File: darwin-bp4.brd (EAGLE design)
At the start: 95 x 128 mm, 25 parts, among them U1 MCP23008, U2 TCA9548A, U3 LP5012

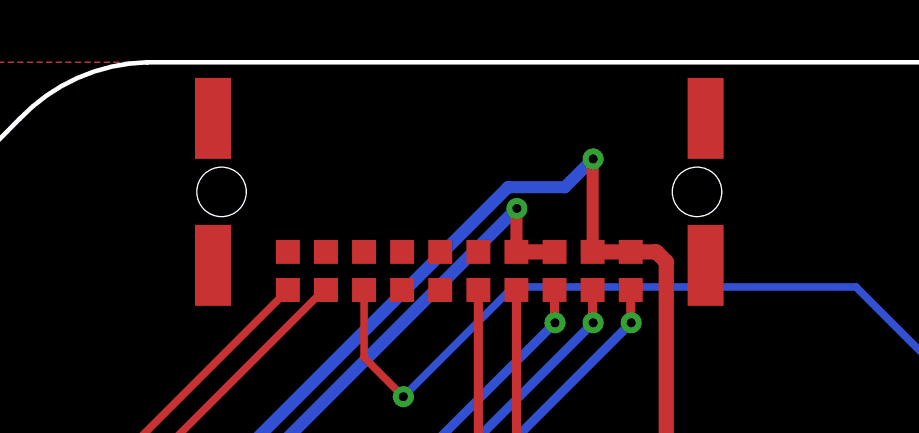
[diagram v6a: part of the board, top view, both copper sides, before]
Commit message: Fixed updated connector footprint.
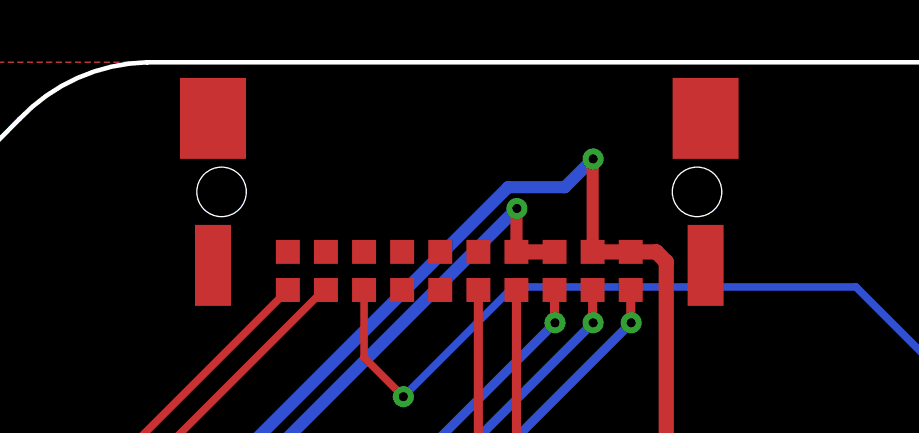
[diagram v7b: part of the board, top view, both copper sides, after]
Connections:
- net GND: now also MEZZ-TO-RADIO.PAD0, MEZZ-TO-RADIO.PAD1, MEZZ-TO-RADIO.PAD2, MEZZ-TO-RADIO.PAD3
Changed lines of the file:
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@@
 </autorouter>
 <elements>
-<element name="MEZZ-TO-RADIO" library="Conservify" library_urn="urn:adsk.eagle:library:11839183" package="M55-7102042R" package3d_urn="urn:adsk.eagle:package:11853513/2" value="M55-6102042R7102(M)" x="47.0492" y="123.68" smashed="yes" rot="R180"/>
+<element name="MEZZ-TO-RADIO" library="Conservify" library_urn="urn:adsk.eagle:library:11839183" package="M55-7102042R" package3d_urn="urn:adsk.eagle:package:11853513/3" value="M55-6102042R7102(M)" x="47.0492" y="123.68" smashed="yes" rot="R180"/>
 <element name="U1" library="Conservify" library_urn="urn:adsk.eagle:library:11839183" package="SOIC18-W" package3d_urn="urn:adsk.eagle:package:11763623/2" value="MCP23008" x="86.8296" y="64.074" smashed="yes" rot="R180">
 <attribute name="VALUE" x="86.8296" y="70.574" size="0.8" layer="27" ratio="20" rot="R180" align="center"/>
@@
 <element name="R1" library="rcl" library_urn="urn:adsk.eagle:library:334" package="R0603" package3d_urn="urn:adsk.eagle:package:23555/3" value="4.7k" x="51.128" y="108.776" smashed="yes">
 <attribute name="NAME" x="53.733" y="108.741" size="0.8" layer="25" ratio="20" align="center"/>
+<attribute name="POPULARITY" value="77" x="51.128" y="108.776" size="1.778" layer="27" display="off"/>
 <attribute name="SPICEPREFIX" value="R" x="51.128" y="108.776" size="1.778" layer="27" display="off"/>
 </element>
 <element name="R2" library="rcl" library_urn="urn:adsk.eagle:library:334" package="R0603" package3d_urn="urn:adsk.eagle:package:23555/3" value="4.7k" x="45.286" y="108.776" smashed="yes" rot="R180">
 <attribute name="NAME" x="42.681" y="108.811" size="0.8" layer="25" ratio="20" rot="R180" align="center"/>
+<attribute name="POPULARITY" value="77" x="45.286" y="108.776" size="1.778" layer="27" rot="R180" display="off"/>
 <attribute name="SPICEPREFIX" value="R" x="45.286" y="108.776" size="1.778" layer="27" rot="R180" display="off"/>
 </element>
 <element name="R3" library="rcl" library_urn="urn:adsk.eagle:library:334" package="R0603" package3d_urn="urn:adsk.eagle:package:23555/3" value="10k" x="89.228" y="72.454" smashed="yes" rot="R180">
 <attribute name="NAME" x="89.223" y="73.989" size="0.8" layer="25" ratio="20" rot="R180" align="center"/>
+<attribute name="POPULARITY" value="77" x="89.228" y="72.454" size="1.778" layer="27" rot="R180" display="off"/>
 <attribute name="SPICEPREFIX" value="R" x="89.228" y="72.454" size="1.778" layer="27" rot="R180" display="off"/>
 </element>
 <element name="R4" library="rcl" library_urn="urn:adsk.eagle:library:334" package="R0603" package3d_urn="urn:adsk.eagle:package:23555/3" value="10k" x="78.052" y="70.168" smashed="yes" rot="R180">
 <attribute name="NAME" x="78.047" y="71.603" size="0.8" layer="25" ratio="20" rot="R180" align="center"/>
+<attribute name="POPULARITY" value="77" x="78.052" y="70.168" size="1.778" layer="27" rot="R180" display="off"/>
 <attribute name="SPICEPREFIX" value="R" x="78.052" y="70.168" size="1.778" layer="27" rot="R180" display="off"/>
 </element>
@@
 <element name="R5" library="rcl" library_urn="urn:adsk.eagle:library:334" package="R0603" package3d_urn="urn:adsk.eagle:package:23555/3" value="4.7k" x="9.9" y="65.3" smashed="yes">
 <attribute name="NAME" x="12.465" y="65.335" size="0.8" layer="25" ratio="20" align="center"/>
+<attribute name="POPULARITY" value="77" x="9.9" y="65.3" size="1.778" layer="27" display="off"/>
 <attribute name="SPICEPREFIX" value="R" x="9.9" y="65.3" size="1.778" layer="27" display="off"/>
 <attribute name="VALUE" x="9.265" y="63.395" size="1.27" layer="27"/>
@@
 <element name="R6" library="rcl" library_urn="urn:adsk.eagle:library:334" package="R0603" package3d_urn="urn:adsk.eagle:package:23555/3" value="100k" x="26.1" y="97.7" smashed="yes">
 <attribute name="NAME" x="28.765" y="97.635" size="0.8" layer="25" rot="R180" align="center"/>
+<attribute name="POPULARITY" value="77" x="26.1" y="97.7" size="1.778" layer="27" display="off"/>
 <attribute name="SPICEPREFIX" value="R" x="26.1" y="97.7" size="0.799996875" layer="27" ratio="20" display="off"/>
 <attribute name="VALUE" x="25.465" y="95.795" size="1.27" layer="27"/>
@@
 <element name="R7" library="rcl" library_urn="urn:adsk.eagle:library:334" package="R0603" package3d_urn="urn:adsk.eagle:package:23555/3" value="100k" x="26" y="71.5" smashed="yes">
 <attribute name="NAME" x="28.765" y="71.435" size="0.8" layer="25" rot="R180" align="center"/>
+<attribute name="POPULARITY" value="77" x="26" y="71.5" size="1.778" layer="27" display="off"/>
 <attribute name="SPICEPREFIX" value="R" x="26" y="71.5" size="0.799996875" layer="27" ratio="20" display="off"/>
 <attribute name="VALUE" x="25.365" y="69.595" size="1.27" layer="27"/>
@@
 <element name="R8" library="rcl" library_urn="urn:adsk.eagle:library:334" package="R0603" package3d_urn="urn:adsk.eagle:package:23555/3" value="100k" x="26" y="45.5" smashed="yes">
 <attribute name="NAME" x="28.665" y="45.535" size="0.8" layer="25" rot="R180" align="center"/>
+<attribute name="POPULARITY" value="77" x="26" y="45.5" size="1.778" layer="27" display="off"/>
 <attribute name="SPICEPREFIX" value="R" x="26" y="45.5" size="0.799996875" layer="27" ratio="20" display="off"/>
 <attribute name="VALUE" x="25.365" y="43.595" size="1.27" layer="27"/>
@@
 <element name="R9" library="rcl" library_urn="urn:adsk.eagle:library:334" package="R0603" package3d_urn="urn:adsk.eagle:package:23555/3" value="100k" x="26" y="19.5" smashed="yes">
 <attribute name="NAME" x="28.665" y="19.535" size="0.8" layer="25" rot="R180" align="center"/>
+<attribute name="POPULARITY" value="77" x="26" y="19.5" size="1.778" layer="27" display="off"/>
 <attribute name="SPICEPREFIX" value="R" x="26" y="19.5" size="0.799996875" layer="27" ratio="20" display="off"/>
 <attribute name="VALUE" x="25.365" y="17.595" size="1.27" layer="27"/>
@@
 <contactref element="R9" pad="2"/>
 <contactref element="U2" pad="PIN12"/>
-<wire x1="68.5" y1="77" x2="68.5" y2="103" width="0" layer="19" extent="1-1"/>
-<wire x1="70.35" y1="67" x2="68.5" y2="77" width="0" layer="19" extent="1-1"/>
-<wire x1="76.85" y1="67" x2="70.35" y2="67" width="0" layer="19" extent="1-1"/>
-<wire x1="77.5" y1="67" x2="76.85" y2="67" width="0" layer="19" extent="1-1"/>
-<wire x1="75.55" y1="61.2" x2="76.85" y2="67" width="0" layer="19" extent="1-1"/>
-<wire x1="79.5" y1="56.125" x2="75.55" y2="61.2" width="0" layer="19" extent="1-1"/>
-<wire x1="81" y1="56.125" x2="79.5" y2="56.125" width="0" layer="19" extent="1-1"/>
-<wire x1="91.4832" y1="61.534" x2="81" y2="56.125" width="0" layer="19" extent="1-1"/>
-<wire x1="91.4832" y1="62.804" x2="91.4832" y2="61.534" width="0" layer="19" extent="1-1"/>
-<wire x1="91.4832" y1="64.074" x2="91.4832" y2="62.804" width="0" layer="19" extent="1-1"/>
-<wire x1="91.4832" y1="69.154" x2="91.4832" y2="64.074" width="0" layer="19" extent="1-1"/>
-<wire x1="68.5" y1="51" x2="79.5" y2="56.125" width="0" layer="19" extent="1-1"/>
-<wire x1="68.5" y1="25" x2="68.5" y2="51" width="0" layer="19" extent="1-1"/>
-<wire x1="42.6042" y1="121.68" x2="68.5" y2="103" width="0" layer="19" extent="1-1"/>
-<wire x1="41.3342" y1="121.68" x2="42.6042" y2="121.68" width="0" layer="19" extent="1-1"/>
-<wire x1="26.95" y1="97.7" x2="41.3342" y2="121.68" width="0" layer="19" extent="1-1"/>
-<wire x1="15" y1="106.81" x2="26.95" y2="97.7" width="0" layer="19" extent="1-1"/>
-<wire x1="15" y1="80.81" x2="26.95" y2="97.7" width="0" layer="19" extent="1-1"/>
-<wire x1="9.675" y1="67" x2="15" y2="80.81" width="0" layer="19" extent="1-1"/>
-<wire x1="10.75" y1="65.3" x2="9.675" y2="67" width="0" layer="19" extent="1-1"/>
-<wire x1="6.5" y1="64.5" x2="9.675" y2="67" width="0" layer="19" extent="1-1"/>
-<wire x1="6" y1="64" x2="6.5" y2="64.5" width="0" layer="19" extent="1-1"/>
-<wire x1="5.5" y1="64.5" x2="6" y2="64" width="0" layer="19" extent="1-1"/>
-<wire x1="6.5" y1="63.5" x2="6" y2="64" width="0" layer="19" extent="1-1"/>
-<wire x1="5.5" y1="63.5" x2="6" y2="64" width="0" layer="19" extent="1-1"/>
-<wire x1="6.4" y1="62.3654" x2="6.5" y2="63.5" width="0" layer="19" extent="1-1"/>
-<wire x1="6.8" y1="62.3654" x2="6.4" y2="62.3654" width="0" layer="19" extent="1-1"/>
-<wire x1="8.4" y1="60.525" x2="6.8" y2="62.3654" width="0" layer="19" extent="1-1"/>
-<wire x1="15" y1="54.81" x2="8.4" y2="60.525" width="0" layer="19" extent="1-1"/>
-<wire x1="26.85" y1="71.5" x2="15" y2="80.81" width="0" layer="19" extent="1-1"/>
-<wire x1="26.85" y1="45.5" x2="15" y2="54.81" width="0" layer="19" extent="1-1"/>
-<wire x1="15" y1="28.81" x2="26.85" y2="45.5" width="0" layer="19" extent="1-1"/>
-<wire x1="26.85" y1="19.5" x2="15" y2="28.81" width="0" layer="19" extent="1-1"/>
+<contactref element="MEZZ-TO-RADIO" pad="PAD3"/>
+<contactref element="MEZZ-TO-RADIO" pad="PAD0"/>
+<contactref element="MEZZ-TO-RADIO" pad="PAD1"/>
+<contactref element="MEZZ-TO-RADIO" pad="PAD2"/>
+<wire x1="6.5" y1="64.5" x2="6" y2="64" width="0" layer="19" extent="1-1"/>
 </signal>
 <signal name="N$10">
